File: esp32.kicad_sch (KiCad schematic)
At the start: 27 parts, among them U26 SRV05-4, U4 W25Q128, U5 ESP32-S3, Y1 40MHz

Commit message: wip
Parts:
- added C13: 10uF, Capacitor_SMD:C_0402_1005Metric, symbol Device:C_Small
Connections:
- net +3V3: now also C13.2
- net GND: now also C13.1
- net PWR_EN: now also U5.43 (GPIO38); no longer U5.9 (GPIO4)
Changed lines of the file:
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@@
   (junction (at 44.45 78.74) (diameter 0) (color 0 0 0 0)
   )
-  (junction (at 81.28 52.07) (diameter 0) (color 0 0 0 0)
-  )
   (junction (at 171.45 97.79) (diameter 0) (color 0 0 0 0)
   )
@@
   )
   (junction (at 31.75 68.58) (diameter 0) (color 0 0 0 0)
+  )
+  (junction (at 62.23 52.07) (diameter 0) (color 0 0 0 0)
+  )
+  (junction (at 74.93 52.07) (diameter 0) (color 0 0 0 0)
   )
   (junction (at 62.23 38.1) (diameter 0) (color 0 0 0 0)
@@
   (no_connect (at 102.87 76.2))
   (no_connect (at 102.87 138.43))
-  (no_connect (at 102.87 143.51))
+  (no_connect (at 102.87 90.17))
   (no_connect (at 67.31 93.98))
   (no_connect (at 67.31 88.9))
@@
     (stroke (width 0) (type default))
   )
-  (wire (pts (xy 102.87 90.17) (xy 113.03 90.17))
+  (wire (pts (xy 102.87 143.51) (xy 113.03 143.51))
     (stroke (width 0) (type default))
   )
@@
     (stroke (width 0) (type default))
   )
+  (wire (pts (xy 62.23 52.07) (xy 62.23 53.34))
+    (stroke (width 0) (type default))
+  )
   (wire (pts (xy 43.18 74.93) (xy 43.18 82.55))
     (stroke (width 0) (type default))
@@
     (stroke (width 0) (type default))
   )
+  (wire (pts (xy 57.15 52.07) (xy 62.23 52.07))
+    (stroke (width 0) (type default))
+  )
   (wire (pts (xy 124.46 55.88) (xy 123.19 55.88))
     (stroke (width 0) (type default))
@@
     (stroke (width 0) (type default))
   )
+  (wire (pts (xy 62.23 52.07) (xy 74.93 52.07))
+    (stroke (width 0) (type default))
+  )
   (wire (pts (xy 74.93 52.07) (xy 81.28 52.07))
     (stroke (width 0) (type default))
@@
     (stroke (width 0) (type default))
   )
-  (wire (pts (xy 81.28 50.8) (xy 81.28 52.07))
+  (wire (pts (xy 57.15 50.8) (xy 57.15 52.07))
     (stroke (width 0) (type default))
   )
@@
   )
   (wire (pts (xy 67.31 76.2) (xy 52.07 76.2))
+    (stroke (width 0) (type default))
+  )
+  (wire (pts (xy 62.23 58.42) (xy 62.23 59.69))
     (stroke (width 0) (type default))
   )
@@
     (effects (font (size 1.27 1.27)) (justify left))
   )
-  (hierarchical_label "PWR_EN" (shape output) (at 113.03 90.17 0) (fields_autoplaced)
+  (hierarchical_label "PWR_EN" (shape output) (at 113.03 143.51 0) (fields_autoplaced)
     (effects (font (size 1.27 1.27)) (justify left))
   )
@@
         (path "/c0b8a503-1da4-4e1a-941c-dddf39a5c519/2d7ad3ad-5e88-44f5-86dc-1521acbc3a27"
           (reference "#PWR025") (unit 1)
+        )
+      )
+    )
+  )
+  (symbol (lib_id "Device:C_Small") (at 62.23 55.88 0) (mirror x) (unit 1)
+    (in_bom yes) (on_board yes) (dnp no) (fields_autoplaced)
+    (property "Reference" "C13" (at 59.9059 55.2299 0)
+      (effects (font (size 1.27 1.27)) (justify right))
+    )
+    (property "Value" "10uF" (at 59.9059 57.1509 0)
+      (effects (font (size 1.27 1.27)) (justify right))
+    )
+    (property "Footprint" "Capacitor_SMD:C_0402_1005Metric" (at 62.23 55.88 0)
+      (effects (font (size 1.27 1.27)) hide)
+    )
+    (property "Datasheet" "~" (at 62.23 55.88 0)
+      (effects (font (size 1.27 1.27)) hide)
+    )
+    (property "LCSC" "C15525" (at 62.23 55.88 0)
+      (effects (font (size 1.27 1.27)) hide)
+    )
+    (pin "1")
+    (pin "2")
+    (instances
+      (project "oled-nametag"
+        (path "/c0b8a503-1da4-4e1a-941c-dddf39a5c519"
+          (reference "C13") (unit 1)
+        )
+        (path "/c0b8a503-1da4-4e1a-941c-dddf39a5c519/2d7ad3ad-5e88-44f5-86dc-1521acbc3a27"
+          (reference "C26") (unit 1)
         )
       )
@@
     )
   )
+  (symbol (lib_id "power:GND") (at 62.23 59.69 0) (unit 1)
+    (in_bom yes) (on_board yes) (dnp no) (fields_autoplaced)
+    (property "Reference" "#PWR027" (at 62.23 66.04 0)
+      (effects (font (size 1.27 1.27)) hide)
+    )
+    (property "Value" "GND" (at 62.23 63.8255 0)
+      (effects (font (size 1.27 1.27)))
+    )
+    (property "Footprint" "" (at 62.23 59.69 0)
+      (effects (font (size 1.27 1.27)) hide)
+    )
+    (property "Datasheet" "" (at 62.23 59.69 0)
+      (effects (font (size 1.27 1.27)) hide)
+    )
+    (pin "1")
+    (instances
+      (project "oled-nametag"
+        (path "/c0b8a503-1da4-4e1a-941c-dddf39a5c519"
+          (reference "#PWR027") (unit 1)
+        )
+        (path "/c0b8a503-1da4-4e1a-941c-dddf39a5c519/2d7ad3ad-5e88-44f5-86dc-1521acbc3a27"
+          (reference "#PWR075") (unit 1)
+        )
+      )
+    )
+  )
   (symbol (lib_id "Device:C_Small") (at 62.23 41.91 0) (mirror x) (unit 1)
     (in_bom yes) (on_board yes) (dnp no) (fields_autoplaced)
@@
     )
   )
-  (symbol (lib_id "power:+3V3") (at 81.28 50.8 0) (unit 1)
-    (in_bom yes) (on_board yes) (dnp no) (fields_autoplaced)
-    (property "Reference" "#PWR034" (at 81.28 54.61 0)
-      (effects (font (size 1.27 1.27)) hide)
-    )
-    (property "Value" "+3V3" (at 81.28 47.2981 0)
-      (effects (font (size 1.27 1.27)))
-    )
-    (property "Footprint" "" (at 81.28 50.8 0)
-      (effects (font (size 1.27 1.27)) hide)
-    )
-    (property "Datasheet" "" (at 81.28 50.8 0)
-      (effects (font (size 1.27 1.27)) hide)
-    )
+  (symbol (lib_id "power:+3V3") (at 57.15 50.8 0) (unit 1)
+    (in_bom yes) (on_board yes) (dnp no) (fields_autoplaced)
+    (property "Reference" "#PWR034" (at 57.15 54.61 0)
+      (effects (font (size 1.27 1.27)) hide)
+    )
+    (property "Value" "+3V3" (at 57.15 47.2981 0)
+      (effects (font (size 1.27 1.27)))
+    )
+    (property "Footprint" "" (at 57.15 50.8 0)
+      (effects (font (size 1.27 1.27)) hide)
+    )
+    (property "Datasheet" "" (at 57.15 50.8 0)
+      (effects (font (size 1.27 1.27)) hide)
+    )

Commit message: Finish ESP32 fanout
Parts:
- added R26 (x2): 5.1k, Resistor_SMD:R_0402_1005Metric, symbol Device:R_Small
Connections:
- net +3V3: now also R26.1
- net GND: now also R26.2
- net OLED_CLK: now also U5.38 (GPIO33); no longer U5.15 (GPIO10)
- net OLED_CS: now also U5.24 (GPIO18); no longer U5.13 (GPIO8)
- net OLED_DATA: now also U5.41 (GPIO36); no longer U5.16 (GPIO11)
- net OLED_DC: now also U5.39 (GPIO34); no longer U5.14 (GPIO9)
- net OLED_EN: now also U5.19 (GPIO14); no longer U5.17 (GPIO12)
- net OLED_RST: now also U5.27 (GPIO21); no longer U5.12 (GPIO7)
- net PDM_CLK: now also U5.43 (GPIO38); no longer U5.10 (GPIO5)
- net PDM_DATA: now also U5.42 (GPIO37); no longer U5.11 (GPIO6)
- net PWR_EN: now also U5.40 (GPIO35); no longer U5.43 (GPIO38)
- net USB_DET: now also U5.9 (GPIO4); no longer U5.39 (GPIO34)
- net ~{BTN1}: now also U5.17 (GPIO12); no longer U5.24 (GPIO18)
- net ~{BTN2}: now also U5.11 (GPIO6); no longer U5.27 (GPIO21)
- net ~{BTN3}: now also U5.10 (GPIO5); no longer U5.38 (GPIO33)
- net ~{CHRG}: now also U5.6 (GPIO1); no longer U5.18 (GPIO13)
- net ~{STAT2}: now also U5.52 (GPIO46); no longer U5.19 (GPIO14)
- net at U5.5 (GPIO0): now also R26.2
- net at U5.51 (GPIO45): now also R26.1
- net +5V renamed VBUS
- no-connect marks 21 -> 19
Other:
- moved on the sheet: R26, R9, U26

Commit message: Make EDRC happy (mostly)
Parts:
- AE1: symbol Device:Antenna_Shield -> Device:Antenna
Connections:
- net GND: no longer AE1.2 (Shield)
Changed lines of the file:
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@@
-    (stroke (width 0) (type default))
-  )
-  (wire (pts (xy 116.84 48.26) (xy 116.84 49.53))
     (stroke (width 0) (type default))
   )
@@
   )
   (wire (pts (xy 133.35 87.63) (xy 134.62 87.63))
+    (stroke (width 0) (type default))
+  )
+  (wire (pts (xy 74.93 36.83) (xy 74.93 38.1))
     (stroke (width 0) (type default))
   )
@@
         (path "/c0b8a503-1da4-4e1a-941c-dddf39a5c519/2d7ad3ad-5e88-44f5-86dc-1521acbc3a27"
           (reference "R7") (unit 1)
-        )
-      )
-    )
-  )
-  (symbol (lib_id "power:GND") (at 116.84 49.53 0) (unit 1)
-    (in_bom yes) (on_board yes) (dnp no) (fields_autoplaced)
-    (property "Reference" "#PWR038" (at 116.84 55.88 0)
-      (effects (font (size 1.27 1.27)) hide)
-    )
-    (property "Value" "GND" (at 116.84 53.6655 0)
-      (effects (font (size 1.27 1.27)))
-    )
-    (property "Footprint" "" (at 116.84 49.53 0)
-      (effects (font (size 1.27 1.27)) hide)
-    )
-    (property "Datasheet" "" (at 116.84 49.53 0)
-      (effects (font (size 1.27 1.27)) hide)
-    )
-    (pin "1")
-    (instances
-      (project "oled-nametag"
-        (path "/c0b8a503-1da4-4e1a-941c-dddf39a5c519"
-          (reference "#PWR038") (unit 1)
-        )
-        (path "/c0b8a503-1da4-4e1a-941c-dddf39a5c519/2d7ad3ad-5e88-44f5-86dc-1521acbc3a27"
-          (reference "#PWR035") (unit 1)
         )
       )
@@
     )
   )
+  (symbol (lib_id "power:PWR_FLAG") (at 74.93 36.83 0) (unit 1)
+    (in_bom yes) (on_board yes) (dnp no) (fields_autoplaced)
+    (property "Reference" "#FLG010" (at 74.93 34.925 0)
+      (effects (font (size 1.27 1.27)) hide)
+    )
+    (property "Value" "PWR_FLAG" (at 74.93 33.3281 0)
+      (effects (font (size 1.27 1.27)))
+    )
+    (property "Footprint" "" (at 74.93 36.83 0)
+      (effects (font (size 1.27 1.27)) hide)
+    )
+    (property "Datasheet" "~" (at 74.93 36.83 0)
+      (effects (font (size 1.27 1.27)) hide)
+    )
+    (pin "1")
+    (instances
+      (project "oled-nametag"
+        (path "/c0b8a503-1da4-4e1a-941c-dddf39a5c519/2d7ad3ad-5e88-44f5-86dc-1521acbc3a27"
+          (reference "#FLG010") (unit 1)
+        )
+      )
+    )
+  )
   (symbol (lib_id "Device:C_Small") (at 62.23 41.91 0) (mirror x) (unit 1)
     (in_bom yes) (on_board yes) (dnp no) (fields_autoplaced)
@@
     )
   )
-  (symbol (lib_id "Device:Antenna_Shield") (at 114.3 43.18 0) (unit 1)
+  (symbol (lib_id "Device:Antenna") (at 114.3 43.18 0) (unit 1)
     (in_bom yes) (on_board yes) (dnp no) (fields_autoplaced)
     (property "Reference" "AE1" (at 117.475 41.9013 0)
@@
       (effects (font (size 1.27 1.27)) (justify left))
     )
-    (property "Footprint" "Antenna_SMD_Molex:2065130001" (at 114.3 40.64 0)
-      (effects (font (size 1.27 1.27)) hide)
-    )
-    (property "Datasheet" "~" (at 114.3 40.64 0)
-      (effects (font (size 1.27 1.27)) hide)
-    )
-    (pin "1")
-    (pin "2")
-    (instances
-      (project "oled-nametag"
+    (property "Footprint" "Antenna_SMD_Molex:2065130001" (at 114.3 43.18 0)
+      (effects (font (size 1.27 1.27)) hide)
+    )
+    (property "Datasheet" "~" (at 114.3 43.18 0)
+      (effects (font (size 1.27 1.27)) hide)
+    )
+    (pin "1")
+    (instances
+      (project "oled-nametag"

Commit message: Add PSRAM
Doom?
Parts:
- added C45: 1uF, Capacitor_SMD:C_0402_1005Metric, symbol Device:C_Small
- added U12: ESP-PSRAM32, Package_SO:SOIC-8_3.9x4.9mm_P1.27mm, symbol Memory_RAM:ESP-PSRAM32
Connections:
- net GND: now also C45.2, U12.4 (VSS)
- net VDD_SPI: now reaches C45.1, U4.8 (VCC), U5.29 (VDD_SPI)
- net VDD_SPI: now also C45.1, U12.8 (VCC)
- net at U5.28 (SPICS1): now also U12.1 (~{CE})
- net at U4.7 (IO3), U5.30 (SPIHD): now also U12.7 (SIO3)
- net at U4.3 (IO2), U5.31 (SPIWP): now also U12.3 (SIO2)
- net at U4.6 (CLK), U5.33 (SPICLK): now also U12.6 (SCLK)
- net at U4.2 (DO(IO1)), U5.34 (SPIQ): now also U12.2 (SO/SIO)
- net at U4.5 (DI(IO0)), U5.35 (SPID): now also U12.5 (SI/SIO)
- no-connect marks 19 -> 18

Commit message: Adjust to new JLC manufacturing requirements
Change default minimum via hole size to .3mm
Replace package thermal vias by .3mm via
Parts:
- U5: footprint Package_DFN_QFN:QFN-56-1EP_7x7mm_P0.4mm_EP4x4mm_ThermalVias -> Package_QFN_ESP32:QFN-56-1EP_7x7mm_P0.4mm_EP4x4mm_ThermalVias_0.3mm
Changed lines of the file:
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@@
       (effects (font (size 1.27 1.27)) (justify left))
     )
-    (property "Footprint" "Package_DFN_QFN:QFN-56-1EP_7x7mm_P0.4mm_EP4x4mm_ThermalVias" (at 100.33 69.85 0)
+    (property "Footprint" "Package_QFN_ESP32:QFN-56-1EP_7x7mm_P0.4mm_EP4x4mm_ThermalVias_0.3mm" (at 100.33 69.85 0)
       (effects (font (size 1.27 1.27)) hide)
     )

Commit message: Start rev1.1
Fixed bugs:
 - Swapped D+ and D-
 - Insufficient pull-down strength on VBUS
 - Default OLED to 4-wire SPI
 - Swap VBUS detect divider from 2/3 to 1/3
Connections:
- net D+: now also U26.4 (IO3), U5.26 (GPIO20); no longer U26.6 (IO4), U5.25 (GPIO19)
- net D-: now also U26.6 (IO4), U5.25 (GPIO19); no longer U26.4 (IO3), U5.26 (GPIO20)
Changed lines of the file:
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@@
     (effects (font (size 1.27 1.27)) (justify left bottom))
   )
-  (label "D+" (at 111.76 123.19 180) (fields_autoplaced)
+  (label "D+" (at 111.76 125.73 180) (fields_autoplaced)
     (effects (font (size 1.27 1.27)) (justify right bottom))
   )
-  (label "D-" (at 111.76 125.73 180) (fields_autoplaced)
+  (label "D-" (at 111.76 123.19 180) (fields_autoplaced)
     (effects (font (size 1.27 1.27)) (justify right bottom))
   )
@@
     (effects (font (size 1.27 1.27)) (justify left))
   )
-  (hierarchical_label "D+" (shape bidirectional) (at 137.16 123.19 0) (fields_autoplaced)
+  (hierarchical_label "D+" (shape bidirectional) (at 137.16 125.73 0) (fields_autoplaced)
     (effects (font (size 1.27 1.27)) (justify left))
   )
@@
     (effects (font (size 1.27 1.27)) (justify left))
   )
-  (hierarchical_label "D-" (shape bidirectional) (at 137.16 125.73 0) (fields_autoplaced)
+  (hierarchical_label "D-" (shape bidirectional) (at 137.16 123.19 0) (fields_autoplaced)
     (effects (font (size 1.27 1.27)) (justify left))
   )

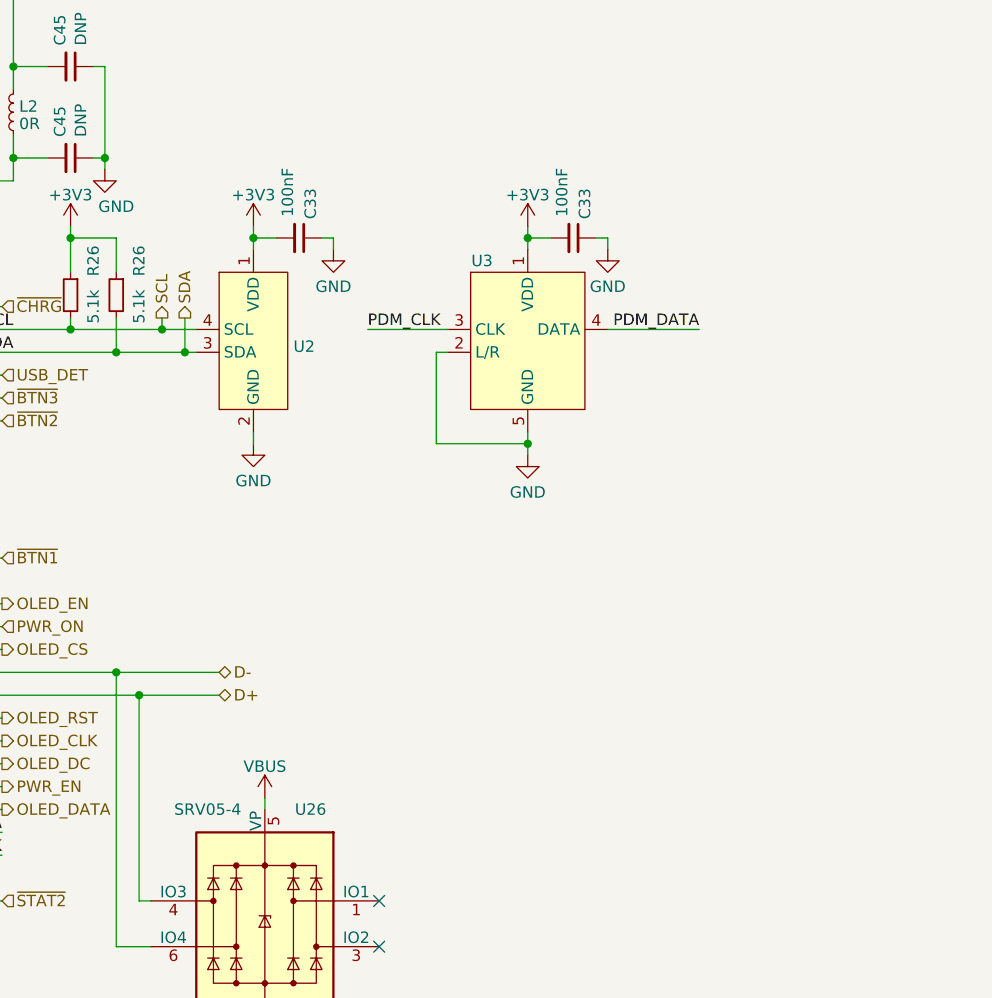
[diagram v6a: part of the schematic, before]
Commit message: Add second light sensor position for reversed device mounting
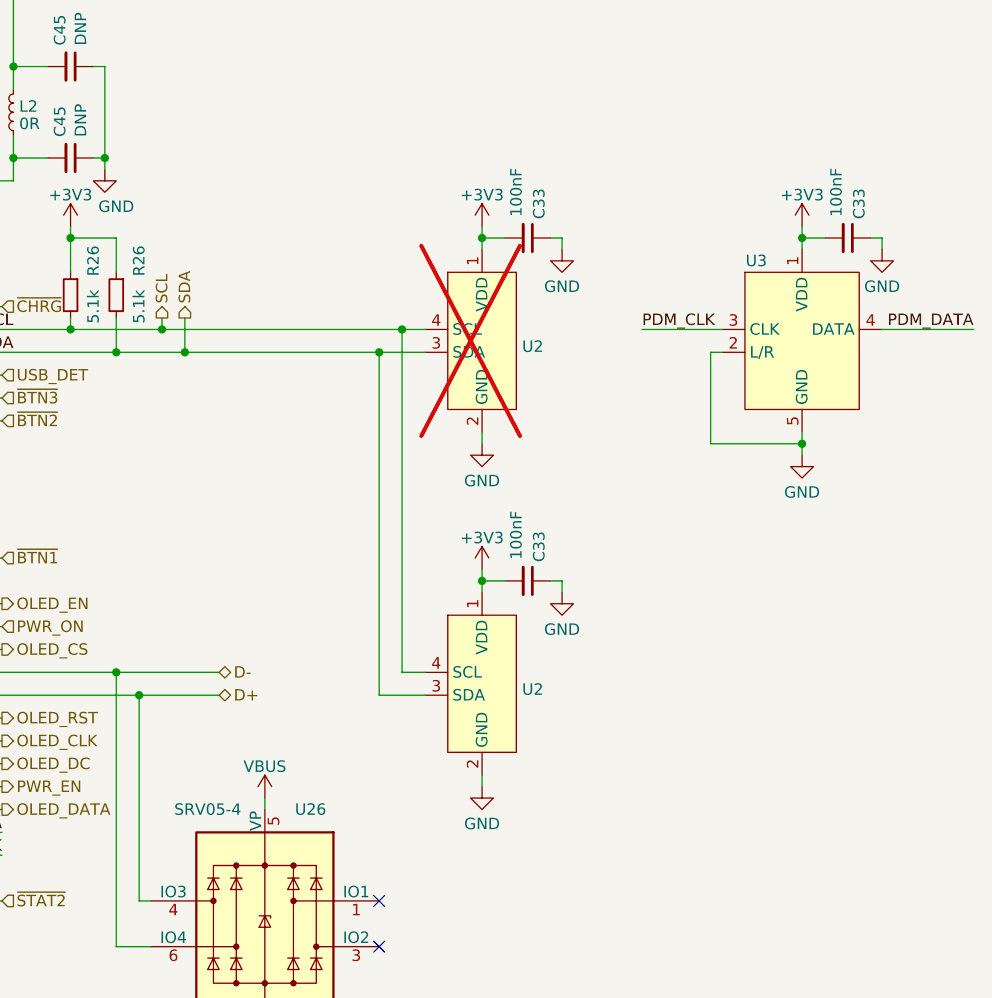
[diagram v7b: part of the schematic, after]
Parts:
- added C33: 100nF, Capacitor_SMD:C_0402_1005Metric, symbol Device:C_Small
- added U2: ~, Sensor_Vishay:VEML3235SL, symbol Sensor_Vishay:VEML3235SL
- U2: now not fitted
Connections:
- net +3V3: now also C33.2, U2.1 (VDD)
- net GND: now also C33.1, U2.2 (GND)
- net SCL: now also U2.4 (SCL)
- net SDA: now also U2.3 (SDA)
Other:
- moved on the sheet: C33, U3

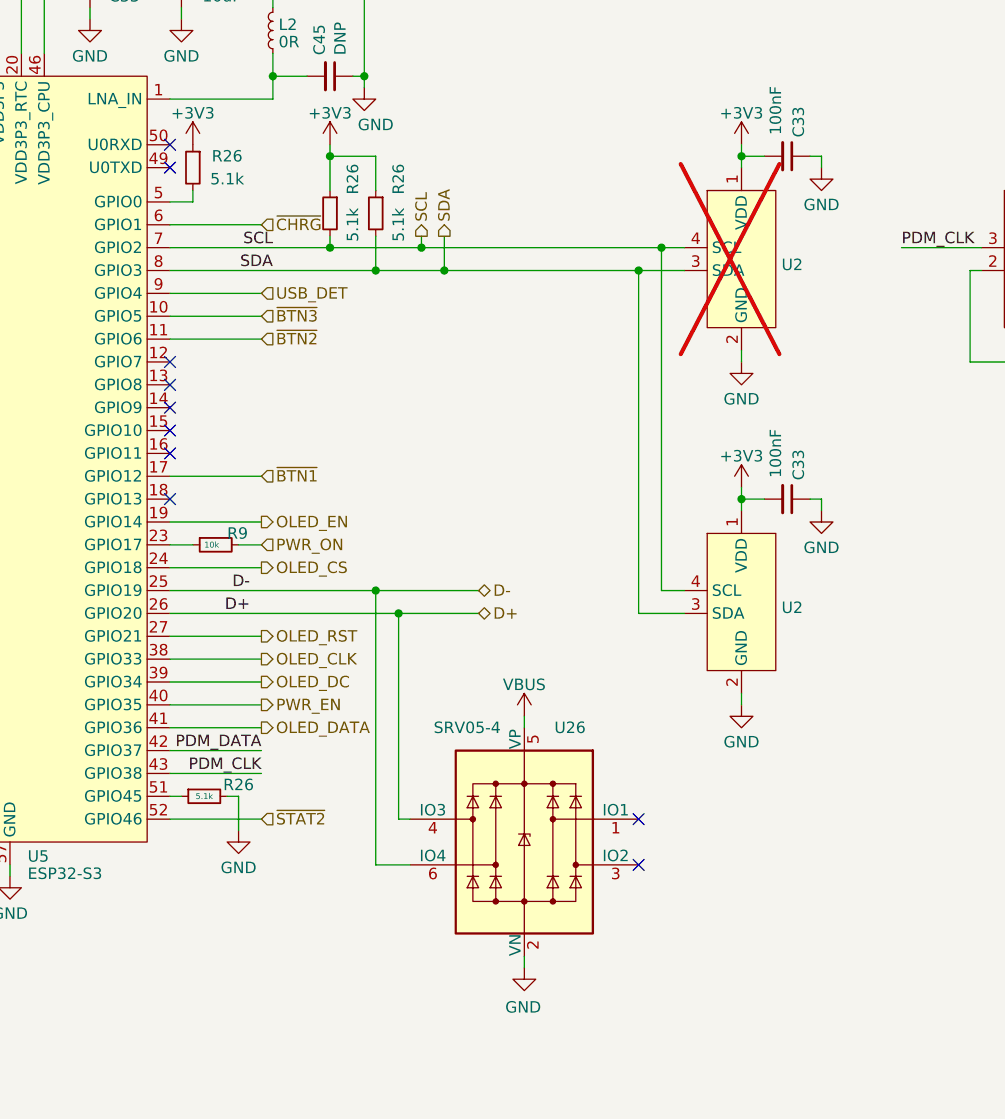
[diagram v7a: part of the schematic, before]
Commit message: Do rough component placement
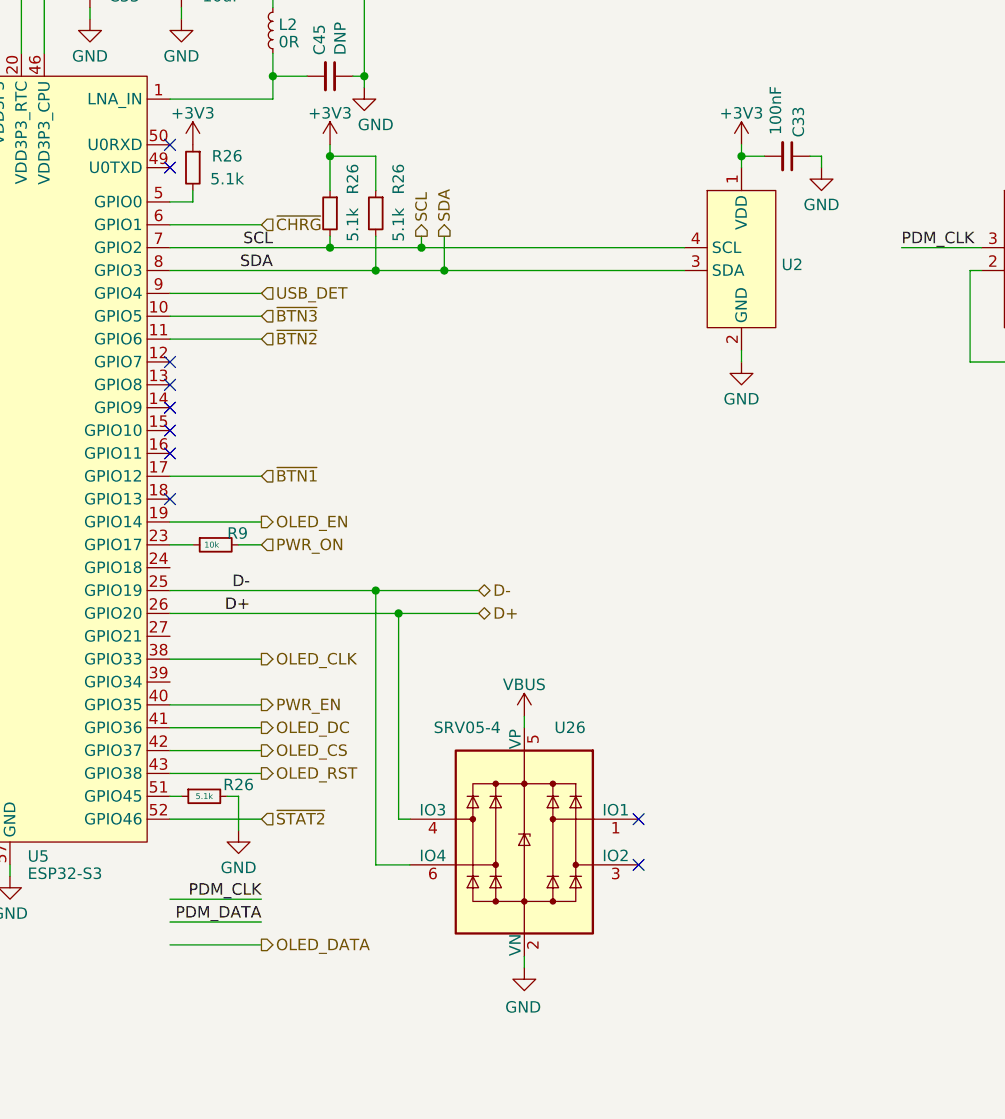
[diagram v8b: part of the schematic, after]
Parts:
- removed C33: 100nF, Capacitor_SMD:C_0402_1005Metric, symbol Device:C_Small
- removed U2: ~, Sensor_Vishay:VEML3235SL, symbol Sensor_Vishay:VEML3235SL
- U2: now fitted
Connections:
- net OLED_CS: now also U5.42 (GPIO37); no longer U5.24 (GPIO18)
- net OLED_DATA: no longer U5.41 (GPIO36)
- net OLED_DC: now also U5.41 (GPIO36); no longer U5.39 (GPIO34)
- net OLED_RST: now also U5.43 (GPIO38); no longer U5.27 (GPIO21)
- net PDM_CLK: no longer U5.43 (GPIO38)
- net PDM_DATA: no longer U5.42 (GPIO37)
